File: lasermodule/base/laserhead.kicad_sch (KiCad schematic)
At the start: 39 parts, among them J3 Conn_01x02, J4 Conn_01x03, J5 Conn_01x02, J6 jumper wire 2 pin, U1 DIGIPOT_50K, U11 LM7808_TO220, U2 U_IC-HKB, U3 STSPIN230, U4 MIC920, U5 MIC920, U6 DRV5033FAxDBZ, U7 DRV5033FAxDBZ, U8 DRV5033FAxDBZ

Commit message: board almost fully synced close for release
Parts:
- removed C5, C9: 10nF, Capacitor_SMD:C_0805_2012Metric_Pad1.18x1.45mm_HandSolder, symbol Device:C
- removed C7: 100nF, Capacitor_SMD:C_0805_2012Metric_Pad1.18x1.45mm_HandSolder, symbol Device:C
- removed J3, J5: Conn_01x02, sockets_scanhead:PinHeader_1x02_P2.54mm_Vertical, symbol Connector_Generic:Conn_01x02
- removed J4: Conn_01x03, sockets_scanhead:pcbmotor_smd, symbol Connector_Generic:Conn_01x03
- removed J6: jumper wire 2 pin, Connector_Molex:Molex_KK-254_AE-6410-02A_1x02_P2.54mm_Vertical, symbol Connector_Generic:Conn_01x02
- removed R14, R15: 10K, Resistor_SMD:R_0805_2012Metric_Pad1.20x1.40mm_HandSolder, symbol Device:R
- removed U11: LM7808_TO220, Package_TO_SOT_THT:TO-220-3_Vertical, symbol Regulator_Linear:LM7805_TO220
- removed U3: STSPIN230, sockets_scanhead:VQFN-16-1EP_3x3mm_P0.5mm_EP1.8x1.8mm, symbol Driver_Motor:STSPIN230
- removed U8: DRV5033FAxDBZ, Package_TO_SOT_SMD:SOT-23, symbol Sensor_Magnetic:DRV5033FAxDBZ
- added J13, J14: Conn_01x01, sockets_scanhead:throughholeplate, symbol Connector_Generic:Conn_01x01
- added U3: DRV5033FAxDBZ, Package_TO_SOT_SMD:SOT-23, symbol Sensor_Magnetic:DRV5033FAxDBZ
- U1: Mouser (none) -> 700-MAX5395MATA+T; Price (none) -> 2,36; Producer (none) -> MAX5395
- U2: Price (none) -> 2.9; Producer (none) -> iC-HK SO8-TP or ic-hkbmsop8
- U4, U5: Farnell (none) -> 2920854; Mouser (none) -> 998-MIC920YC5TR; Price (none) -> 0,44
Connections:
- net +12V: now also J14.1 (Pin_1)
- net +3V3: now also R4.1, R5.1, U3.1 (VCC)
- net +5V: no longer R4.1, R5.1
- net GND: now also U3.3 (GND)
- net HALL1: now also R13.2, U7.2 (OUT)
- net HALL2: now also R4.2, U3.2 (OUT); no longer R13.2, U6.2 (OUT)
- net HALL3: now also R5.2, U6.2 (OUT); no longer U7.2 (OUT)
- net LDK: now also J13.1 (Pin_1)
- net DiodeK: now reaches C6.2, R7.1, U4.3 (-)
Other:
- note removed: "PCB motor"
- note removed: "pcb motor"
- moved on the sheet: C1, C2, C3, C4, C6, C8, R1, R10, R11, R12, R2, R3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

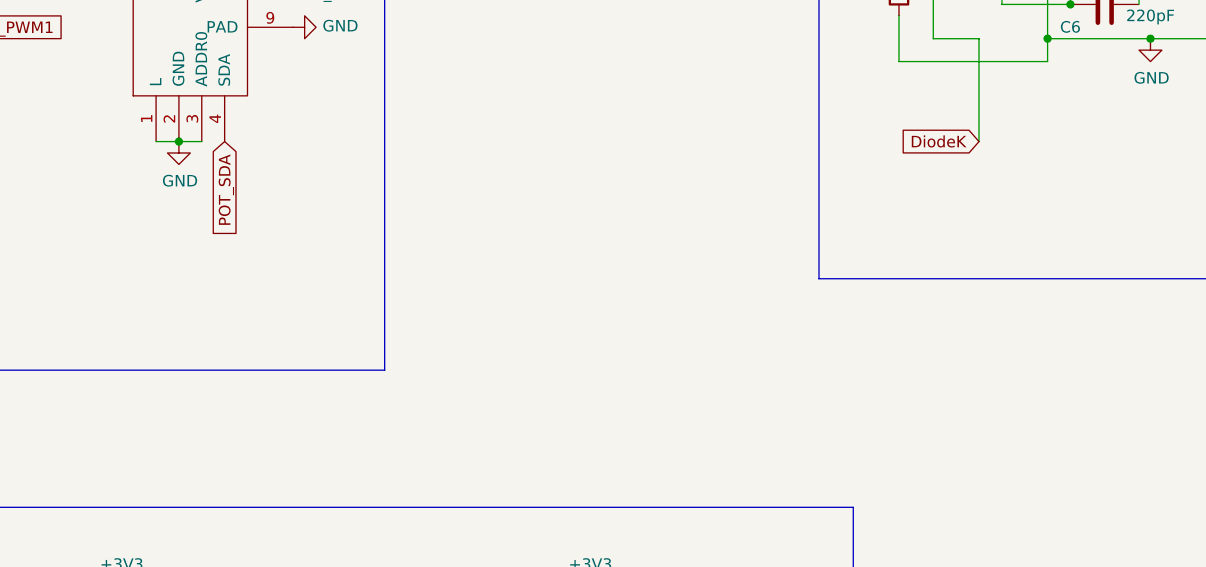
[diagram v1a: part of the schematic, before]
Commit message: added kicost tracking other plates, fixed plates
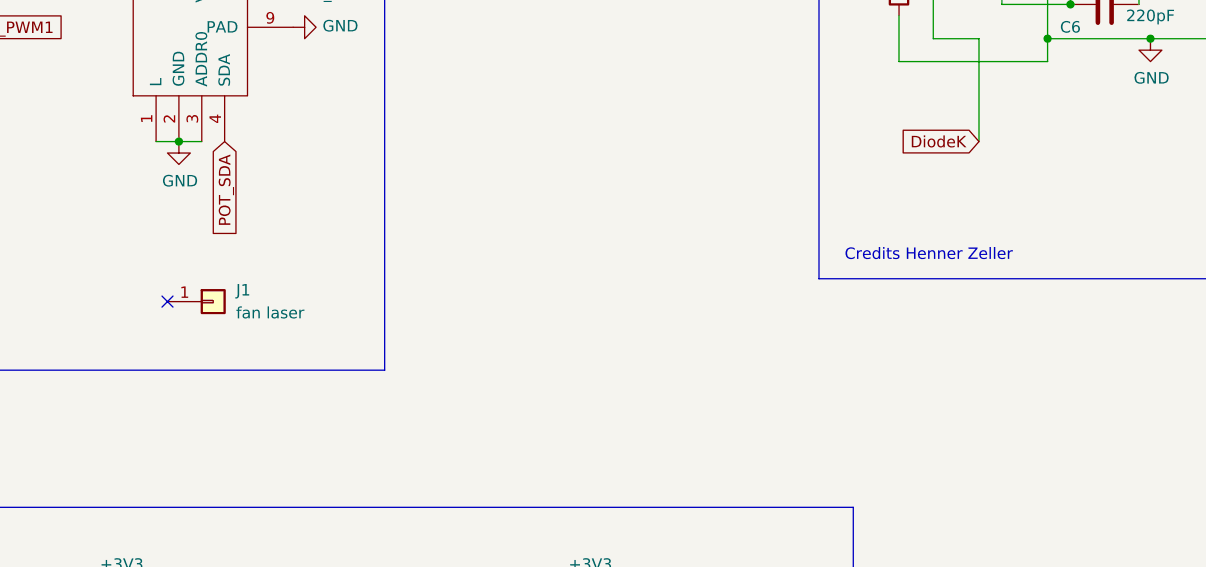
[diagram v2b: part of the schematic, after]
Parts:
- added J1: fan laser, symbol Connector_Generic:Conn_01x01
- C1: manf# (none) -> VJ0805Y473JXXCW1BC; mouser# (none) -> 77-VJ0805Y473JXXCBC
- C2, C3, C8: farnell# (none) -> 2094043; manf# (none) -> 08055C105KAT2A; mouser# (none) -> 581-08055C105KAT2A
- C4: farnell# (none) -> 1414663; manf# (none) -> C0805C104J5RACTU; mouser# (none) -> 80-C0805C104J5R
- C6: manf# (none) -> C0805C221J5GACAUTO; mouser# (none) -> 80-C0805C221J5GAUTO
- R1, R10, R7: manf# (none) -> MCU08050C2202FP500; mouser# (none) -> 594-MCU08050C2202FP5
- R11: manf# (none) -> CR0805-JW-152ELF; mouser# (none) -> 652-CR0805JW-152ELF
- R12, R6, R8, R9: manf# (none) -> CR0805-FX-8251ELF; mouser# (none) -> 652-CR0805FX-8251ELF
- R13, R2, R3, R4, R5: farnell# (none) -> 2826162; manf# (none) -> CRCW080510K0JNEAC; mouser# (none) -> 71-CRCW080510K0JNEAC
- U1: Mouser 700-MAX5395MATA+T -> (none); Price 2,36 -> (none); Producer MAX5395 -> (none); farnell# (none) -> 2763348; manf# (none) -> MAX5395MATA+T; mouser# (none) -> 700-MAX5395MATA+T
- U2: Price 2.9 -> (none)
- U3, U6, U7: farnell# (none) -> 3006067; manf# (none) -> DRV5033FAQDBZR; mouser# (none) -> 595-RV5033FAEDBZRQ1
- U4, U5: Farnell 2920854 -> (none); Mouser 998-MIC920YC5TR -> (none); Price 0,44 -> (none); farnell# (none) -> 2920854; manf# (none) -> MIC920YC5-TR; mouser# (none) -> 998-MIC920YC5TR
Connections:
- no-connect marks 0 -> 1
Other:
- note added: "Credits Henner Zeller"
- company: (none) -> Hexastorm
- title: (none) -> Laserhead Base

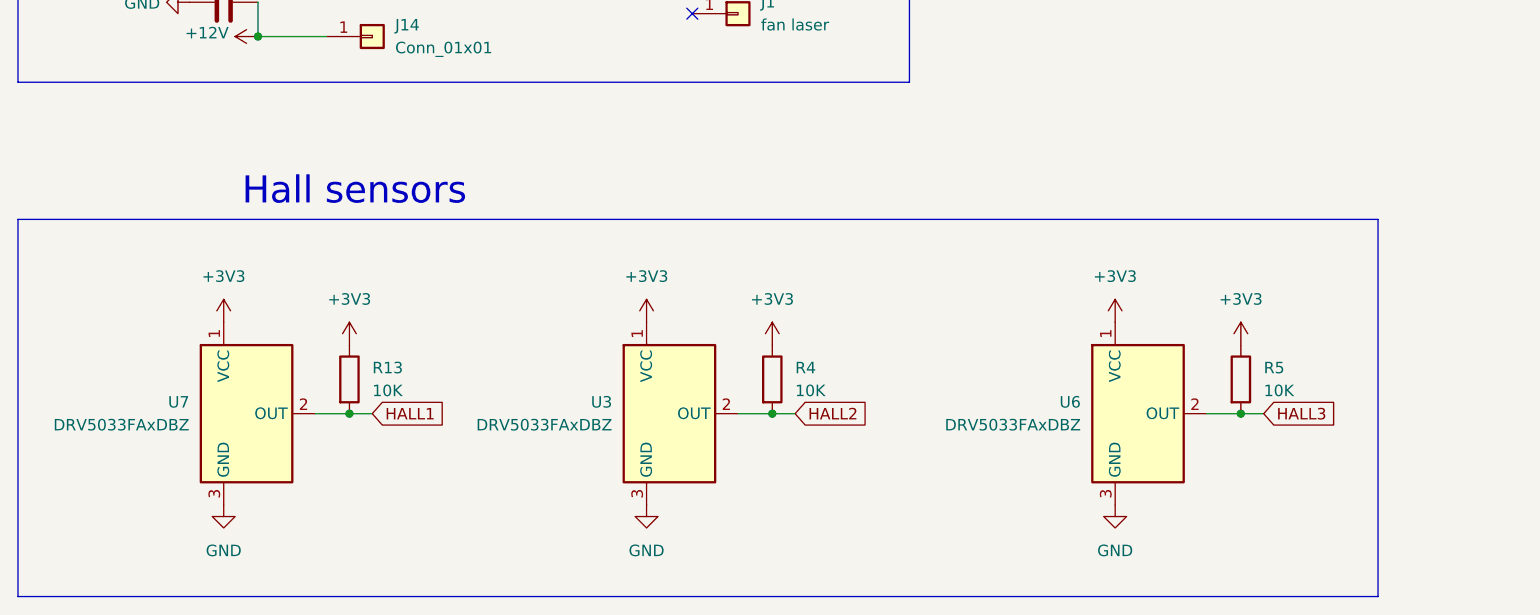
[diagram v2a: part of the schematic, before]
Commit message: improved connection between pcb motor and base plate
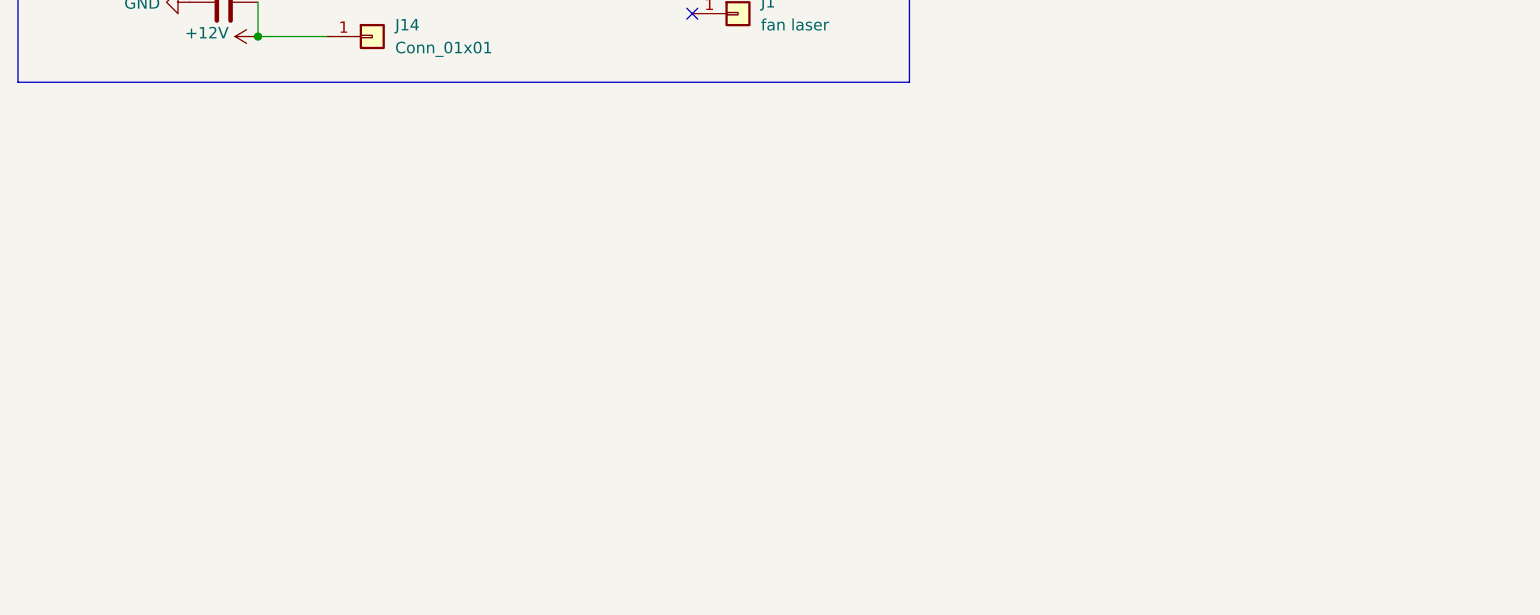
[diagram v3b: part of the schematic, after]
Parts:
- removed R13, R4, R5: 10K, Resistor_SMD:R_0805_2012Metric_Pad1.20x1.40mm_HandSolder, symbol Device:R
- removed U3, U6, U7: DRV5033FAxDBZ, Package_TO_SOT_SMD:SOT-23, symbol Sensor_Magnetic:DRV5033FAxDBZ
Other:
- note removed: "Hall sensors"

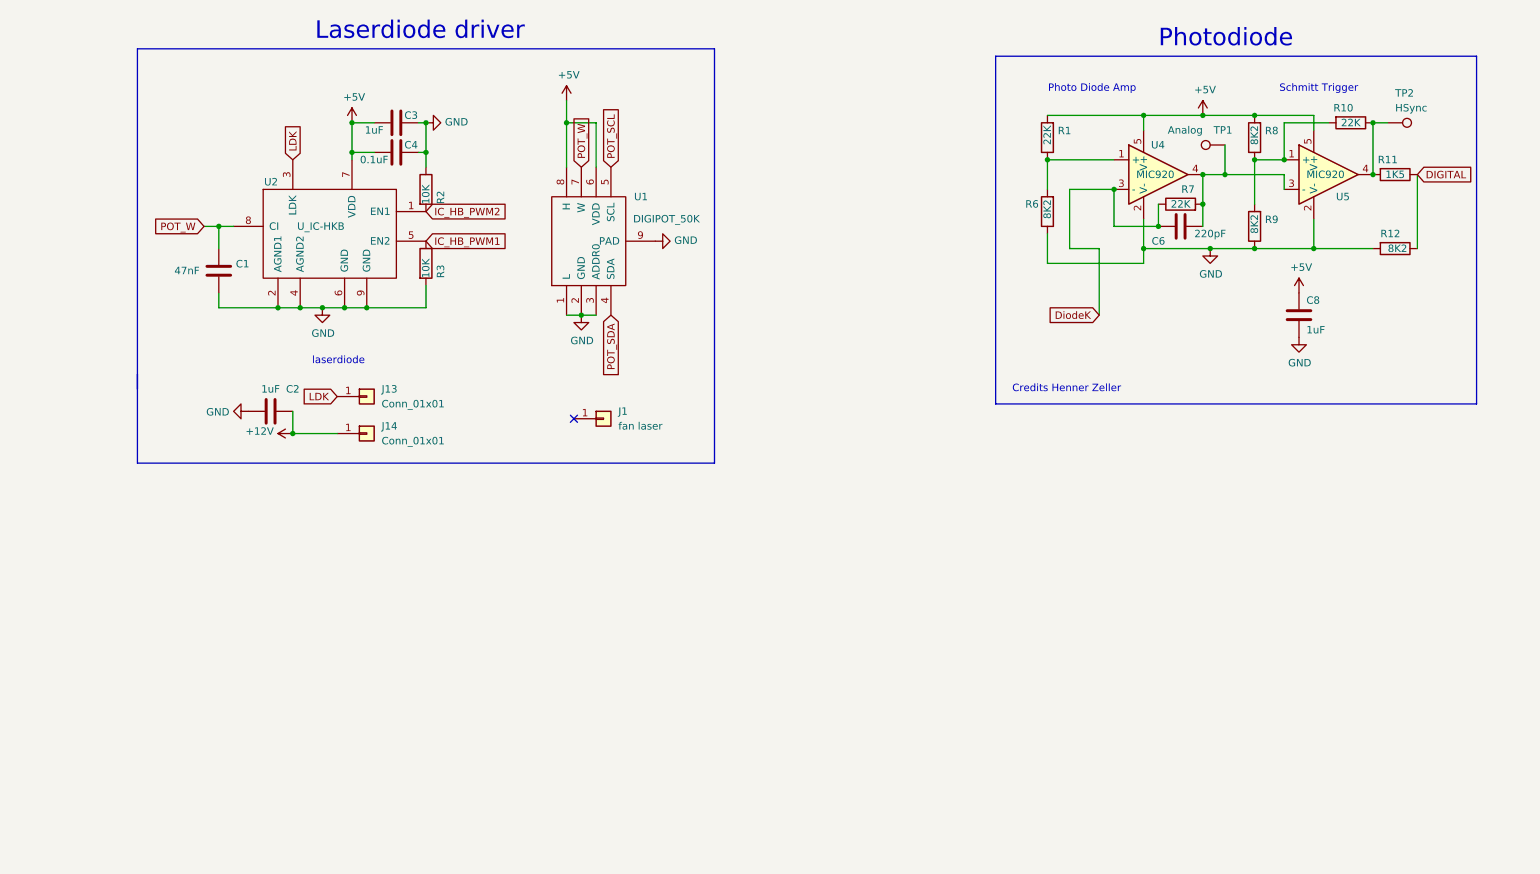
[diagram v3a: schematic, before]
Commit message: added mount felixprinter, standoffs
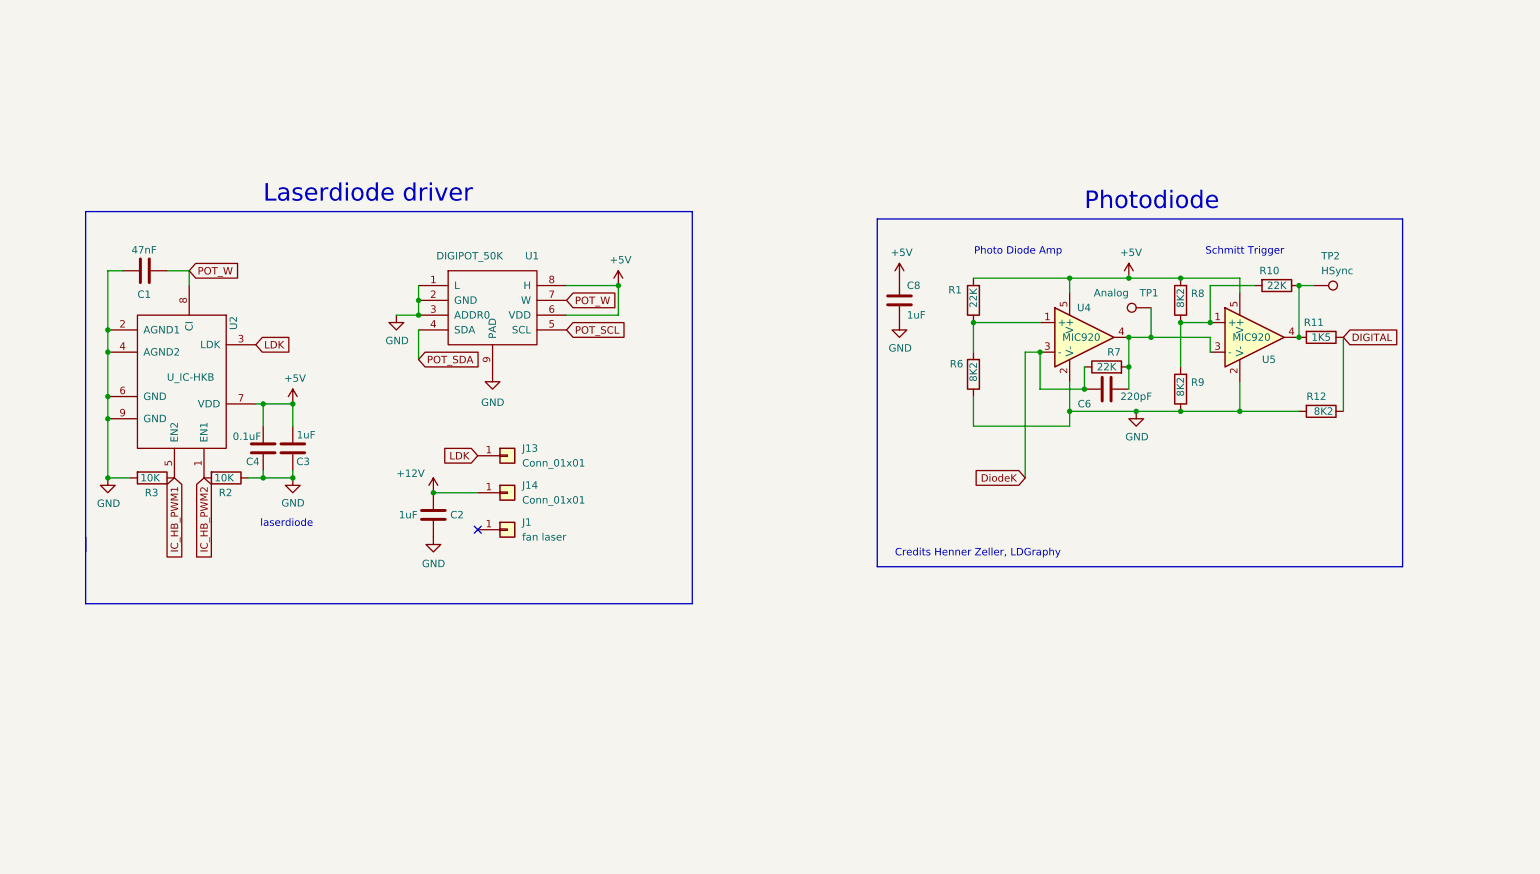
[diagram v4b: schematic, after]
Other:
- note added: "Credits Henner Zeller, LDGraphy"
- note removed: "Credits Henner Zeller"
- moved on the sheet: C1, C2, C3, C4, C6, C8, J1, J13, J14, R1, R10, R11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
